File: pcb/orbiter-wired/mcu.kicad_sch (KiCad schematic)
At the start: 14 parts, among them J1 SWD, J4 AudioJack4, SW1 SW_SPDT

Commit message: Latest schematic
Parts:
- J4: LCSC Part # (none) -> C431535
- MCU1: LCSC Part # (none) -> C81720
- SW1: LCSC Part # (none) -> C221841
- USB_P1: LCSC Part # (none) -> C319148
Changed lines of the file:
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@@
+			)
+		)
+		(property "LCSC Part #" "C431535"
+			(at 128.27 35.56 0)
+			(effects
+				(font
+					(size 1.27 1.27)
+				)
+				(hide yes)
 			)
 		)
@@
 			)
 		)
+		(property "LCSC Part #" "C319148"
+			(at 110.49 76.2 0)
+			(effects
+				(font
+					(size 1.27 1.27)
+				)
+				(hide yes)
+			)
+		)
 		(pin "S1"
 		)
@@
 			)
 		)
+		(property "LCSC Part #" "C81720"
+			(at 215.9 60.96 0)
+			(effects
+				(font
+					(size 1.27 1.27)
+				)
+				(hide yes)
+			)
+		)
 		(pin "29"
 		)
@@
 			(at 217.17 146.05 0)
 			(effects
+				(font
+					(size 1.27 1.27)
+				)
+				(hide yes)
+			)
+		)
+		(property "LCSC Part #" "C221841"
+			(at 217.17 146.05 0)
+			(effects

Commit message: Orbiter wired v1.0 gerber & cleanup of old project files
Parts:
- C4: LCSC Part # C19666 -> (none)
- C5, C6, C7, C8, C9: LCSC Part # C1525 -> (none)
- J4: JLCPCB Part # C431535 -> (none); LCSC Part # C431535 -> (none)
- MCU1: JLCPCB Part # C81720 -> (none); LCSC Part # C81720 -> (none)
- R6: LCSC Part # C25744 -> (none)
- SW1: JLCPCB Part # C221841 -> (none); LCSC Part # C221841 -> (none)
- USB_P1: JLCPCB Part # C319148 -> (none); LCSC Part # C319148 -> (none)
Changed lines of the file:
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@@
-			)
-		)
-		(property "LCSC Part #" "C19666"
-			(at 195.58 125.73 0)
-			(effects
-				(font
-					(size 1.27 1.27)
-				)
-				(hide yes)
-			)
-		)
-		(property "JLCPCB Part #" ""
-			(at 195.58 125.73 0)
-			(effects
-				(font
-					(size 1.27 1.27)
-				)
-				(hide yes)
 			)
 		)
@@
 			)
 		)
-		(property "LCSC Part #" "C1525"
-			(at 242.57 125.73 0)
-			(effects
-				(font
-					(size 1.27 1.27)
-				)
-				(hide yes)
-			)
-		)
-		(property "JLCPCB Part #" ""
-			(at 242.57 125.73 0)
-			(effects
-				(font
-					(size 1.27 1.27)
-				)
-				(hide yes)
-			)
-		)
 		(pin "1"
 		)
@@
 			)
 		)
-		(property "LCSC Part #" "C1525"
-			(at 223.52 125.73 0)
-			(effects
-				(font
-					(size 1.27 1.27)
-				)
-				(hide yes)
-			)
-		)
-		(property "JLCPCB Part #" ""
-			(at 223.52 125.73 0)
-			(effects
-				(font
-					(size 1.27 1.27)
-				)
-				(hide yes)
-			)
-		)
 		(pin "1"
 		)
@@
 		)
 		(property "Description" ""
-			(at 233.045 125.73 0)
-			(effects
-				(font
-					(size 1.27 1.27)
-				)
-				(hide yes)
-			)
-		)
-		(property "LCSC Part #" "C1525"
-			(at 233.045 125.73 0)
-			(effects
-				(font
-					(size 1.27 1.27)
-				)
-				(hide yes)
-			)
-		)
-		(property "JLCPCB Part #" ""
 			(at 233.045 125.73 0)
 			(effects
@@
 			)
 		)
-		(property "JLCPCB Part #" "C431535"
-			(at 128.27 35.56 0)
-			(effects
-				(font
-					(size 1.27 1.27)
-				)
-				(hide yes)
-			)
-		)
-		(property "LCSC Part #" "C431535"
-			(at 128.27 35.56 0)
-			(effects
-				(font
-					(size 1.27 1.27)
-				)
-				(hide yes)
-			)
-		)
 		(pin "R2"
 		)
@@
 		)
 		(property "Description" ""
-			(at 85.09 34.29 0)
-			(effects
-				(font
-					(size 1.27 1.27)
-				)
-				(hide yes)
-			)
-		)
-		(property "JLCPCB Part #" ""
 			(at 85.09 34.29 0)
 			(effects
@@
 			)
 		)
-		(property "JLCPCB Part #" ""
-			(at 153.67 34.29 0)
-			(effects
-				(font
-					(size 1.27 1.27)
-				)
-				(hide yes)
-			)
-		)
 		(pin "2"
 		)
@@
 		)
 		(property "Description" ""
-			(at 204.47 125.73 0)
-			(effects
-				(font
-					(size 1.27 1.27)
-				)
-				(hide yes)
-			)
-		)
-		(property "LCSC Part #" "C1525"
-			(at 204.47 125.73 0)
-			(effects
-				(font
-					(size 1.27 1.27)
-				)
-				(hide yes)
-			)
-		)
-		(property "JLCPCB Part #" ""
 			(at 204.47 125.73 0)
 			(effects
@@
 			)
 		)
-		(property "JLCPCB Part #" "C319148"
-			(at 110.49 76.2 0)
-			(effects
-				(font
-					(size 1.27 1.27)
-				)
-				(hide yes)
-			)
-		)
-		(property "LCSC Part #" "C319148"
-			(at 110.49 76.2 0)
-			(effects
-				(font
-					(size 1.27 1.27)
-				)
-				(hide yes)
-			)
-		)
 		(pin "S1"
 		)
@@
 			)
 		)
-		(property "JLCPCB Part #" "C81720"
-			(at 215.9 60.96 0)
-			(effects
-				(font
-					(size 1.27 1.27)
-				)
-				(hide yes)
-			)
-		)
-		(property "LCSC Part #" "C81720"
-			(at 215.9 60.96 0)
-			(effects
-				(font
-					(size 1.27 1.27)
-				)
-				(hide yes)
-			)
-		)
 		(pin "29"
 		)
@@
 			)
 		)
-		(property "LCSC Part #" "C1525"
-			(at 213.995 125.73 0)
-			(effects
-				(font
-					(size 1.27 1.27)
-				)
-				(hide yes)
-			)
-		)
-		(property "JLCPCB Part #" ""
-			(at 213.995 125.73 0)
-			(effects
-				(font
-					(size 1.27 1.27)
-				)
-				(hide yes)
-			)
-		)
 		(pin "2"
 		)
@@
 		)
 		(property "Description" ""
-			(at 209.55 146.05 0)
-			(effects
-				(font
-					(size 1.27 1.27)
-				)
-				(hide yes)
-			)
-		)
-		(property "LCSC Part #" "C25744"
-			(at 209.55 146.05 0)
-			(effects
-				(font
-					(size 1.27 1.27)
-				)
-				(hide yes)
-			)
-		)
-		(property "JLCPCB Part #" ""
 			(at 209.55 146.05 0)
 			(effects
@@
 			)
 		)
-		(property "JLCPCB Part #" ""
-			(at 128.27 66.04 0)
-			(effects
-				(font
-					(size 1.27 1.27)
-				)
-				(hide yes)
-			)
-		)
 		(pin "2"
 		)
@@
 			(at 217.17 146.05 0)
 			(effects
-				(font
-					(size 1.27 1.27)
-				)
-				(hide yes)
-			)
-		)
-		(property "JLCPCB Part #" "C221841"
-			(at 217.17 146.05 0)
-			(effects
-				(font
-					(size 1.27 1.27)
-				)
-				(hide yes)
-			)
-		)
-		(property "LCSC Part #" "C221841"
-			(at 217.17 146.05 0)
-			(effects

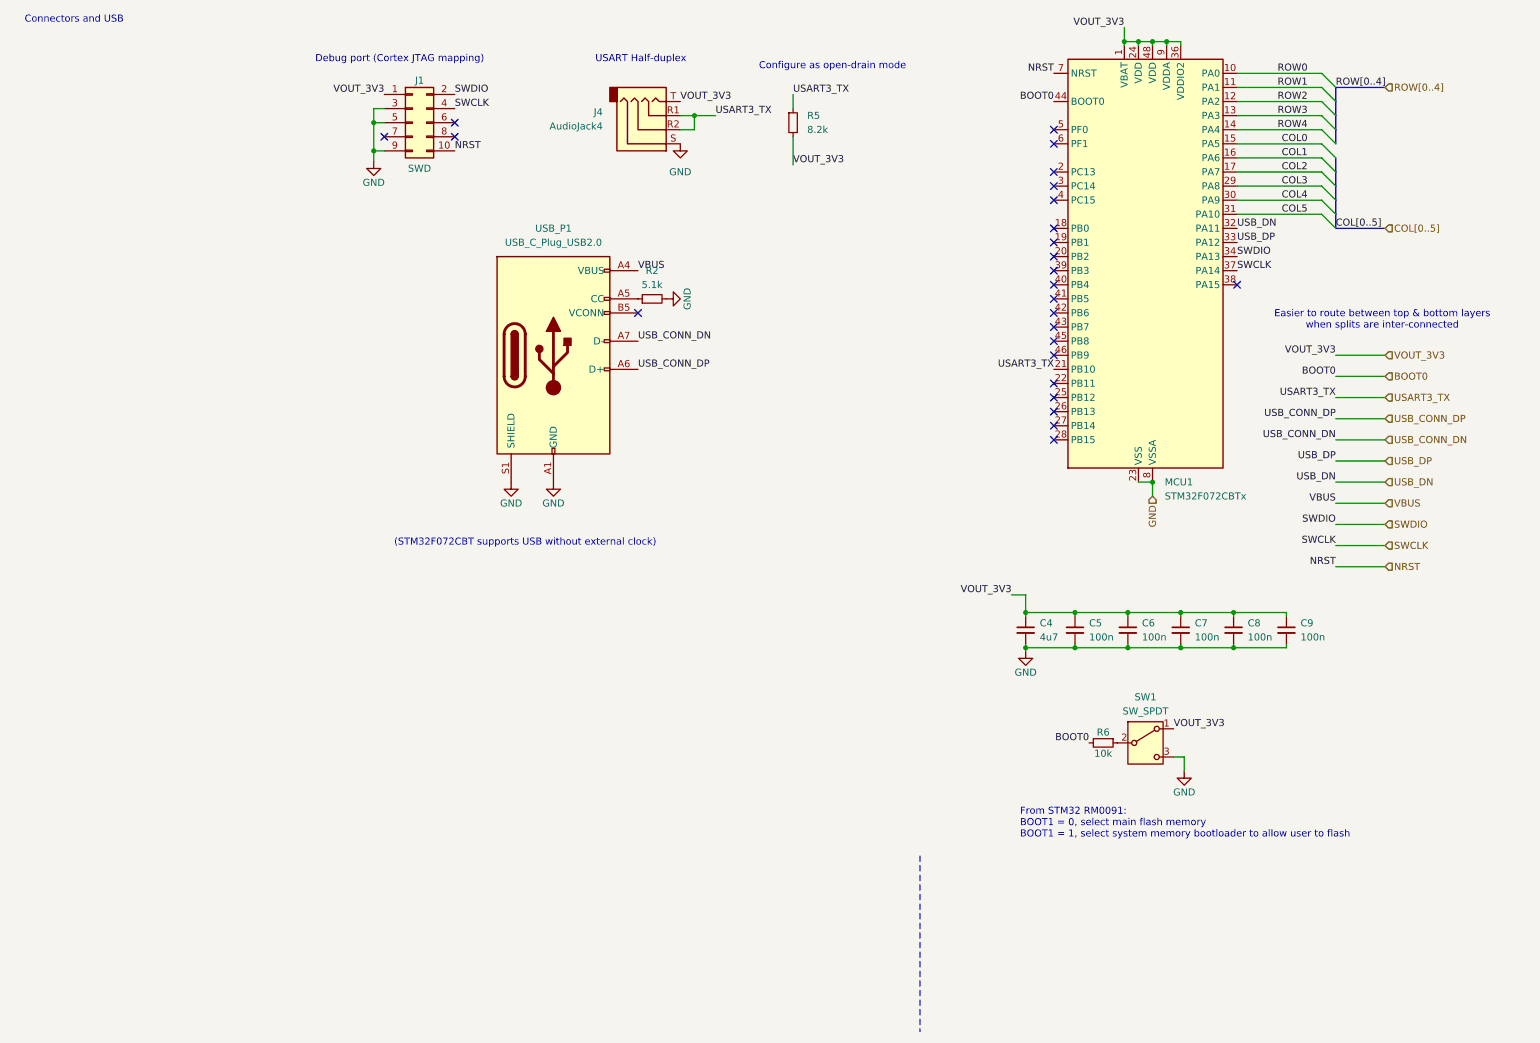
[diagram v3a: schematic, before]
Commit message: WIP prepare component placement for standalone dev pcb
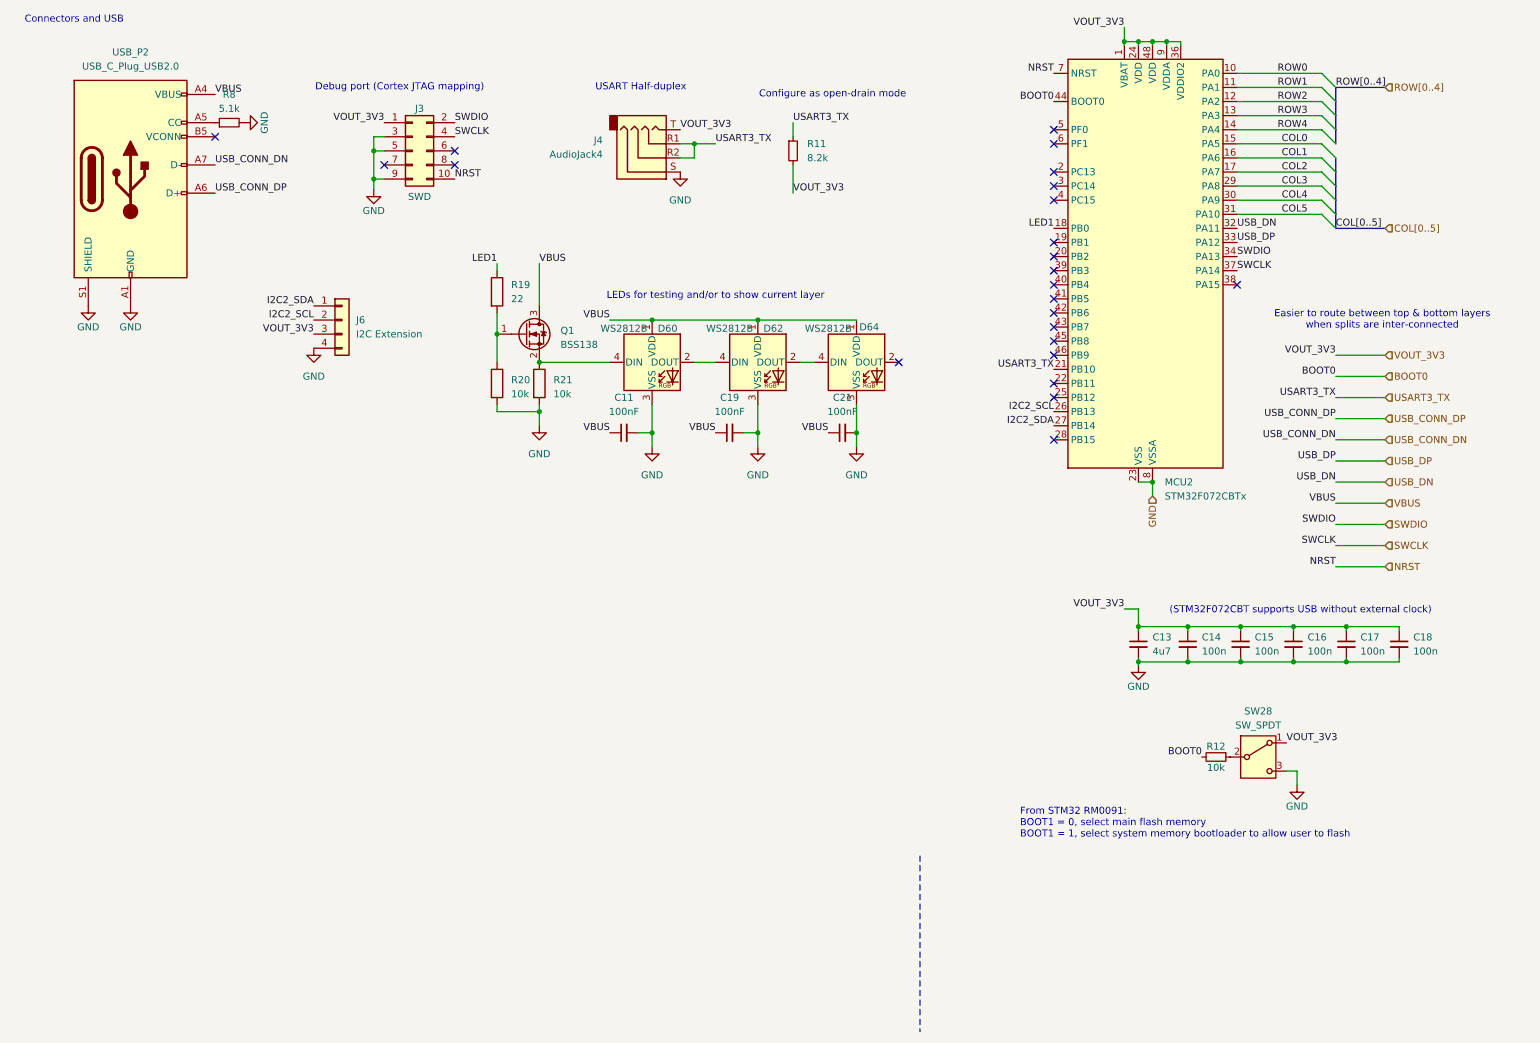
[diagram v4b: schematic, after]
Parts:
- added C11, C19, C21: 100nF, Capacitor_SMD:C_0603_1608Metric_Pad1.08x0.95mm_HandSolder, symbol Device:C_Small
- added D60, D62, D64: WS2812B, LED_SMD:LED_WS2812B-2020_PLCC4_2.0x2.0mm, symbol LED:WS2812B
- added J6: I2C Extension, Connector_PinSocket_1.00mm:PinSocket_1x04_P1.00mm_Vertical_SMD_Pin1Left, symbol Connector_Generic:Conn_01x04
- added Q1: BSS138, Package_TO_SOT_SMD:SOT-23, symbol Transistor_FET:BSS138
- added R19: 22, Resistor_SMD:R_0603_1608Metric, symbol Device:R
- added R20, R21: 10k, Resistor_SMD:R_0603_1608Metric, symbol Device:R
- renumbered C4 to C13, C5 to C14, C6 to C15, C7 to C16, C8 to C17, C9 to C18, J1 to J3, MCU1 to MCU2, R5 to R11, R6 to R12, R2 to R8, SW1 to SW28, USB_P1 to USB_P2
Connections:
- net GND: now also C11.2, C19.2, C21.2, D60.3 (VSS), D62.3 (VSS), D64.3 (VSS), J6.4 (Pin_4), R20.2, R21.2
- net VBUS: now also C11.1, C19.1, C21.1, D60.1 (VDD), D62.1 (VDD), D64.1 (VDD), Q1.3 (D)
- net VOUT_3V3: now also J6.3 (Pin_3)
- net LED1: now reaches MCU2.18 (PB0)
- net LED1: now also R19.1
- net I2C2_SCL: now reaches MCU2.26 (PB13)
- net I2C2_SCL: now also J6.2 (Pin_2)
- net I2C2_SDA: now reaches MCU2.27 (PB14)
- net I2C2_SDA: now also J6.1 (Pin_1)
- new net: Q1.1 (G), R19.2, R20.1
- new net: D60.4 (DIN), Q1.2 (S), R21.1
- new net: D62.2 (DOUT), D64.4 (DIN)
- new net: D60.2 (DOUT), D62.4 (DIN)
- no-connect marks 25 -> 23
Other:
- note added: "LEDs for testing and/or to show current layer"
- moved on the sheet: C13, C14, C15, C16, C17, C18, J3, J4, R11, R12, R8, SW28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

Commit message: Latest WIP
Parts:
- removed J3: SWD, Connector_PinSocket_1.27mm:PinSocket_2x05_P1.27mm_Vertical_SMD, symbol Connector_Generic:Conn_02x05_Odd_Even
- removed J6: I2C Extension, Connector_PinSocket_1.00mm:PinSocket_1x04_P1.00mm_Vertical_SMD_Pin1Left, symbol Connector_Generic:Conn_01x04
- removed R12: 10k, Resistor_SMD:R_0603_1608Metric, symbol Device:R_Small
- removed SW28: SW_SPDT, Button_Switch_SMD:SW_SPDT_PCM12, symbol Switch:SW_SPDT
- added R6: 10k, Resistor_SMD:R_0603_1608Metric, symbol Device:R_Small
- added SW1: SW_SPDT, Button_Switch_SMD:SW_SPDT_PCM12, symbol Switch:SW_SPDT
- renumbered Q1 to Q2
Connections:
- net BOOT0: now also R6.2
- net GND: now also SW1.3 (C)
- net USART3_TX: no longer J4.R2
- net VOUT_3V3: now also SW1.1 (A)
- net USART3_RX: now reaches MCU2.22 (PB11)
- net USART3_RX: now also J4.R2
- new net: R6.1, SW1.2 (B)
- no-connect marks 23 -> 19
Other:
- note removed: "Debug port (Cortex JTAG mapping)"
- moved on the sheet: C13, C14, C15, C16, C17, C18, R8, USB_P2

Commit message: No DRC errors with new clean layout
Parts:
- SW28: renamed from SW1; footprint Button_Switch_SMD:SW_SPDT_PCM12 -> Button_Switch_SMD:SW_SPST_PTS647_Sx38
- renumbered R6 to R7
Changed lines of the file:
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@@
 		(on_board yes)
 		(dnp no)
-		(property "Reference" "#PWR012"
+		(property "Reference" "#PWR018"
 			(at 79.375 134.62 0)
 			(effects
@@
 		(on_board yes)
 		(dnp no)
-		(property "Reference" "R6"
+		(property "Reference" "R7"
 			(at 64.77 121.285 90)
 			(effects
@@
 		(on_board yes)
 		(dnp no)
-		(property "Reference" "SW1"
+		(property "Reference" "SW28"
 			(at 72.39 114.935 0)
 			(effects
@@
 			)
 		)
-		(property "Footprint" "Button_Switch_SMD:SW_SPDT_PCM12"
+		(property "Footprint" "Button_Switch_SMD:SW_SPST_PTS647_Sx38"
 			(at 72.39 123.19 0)
 			(effects

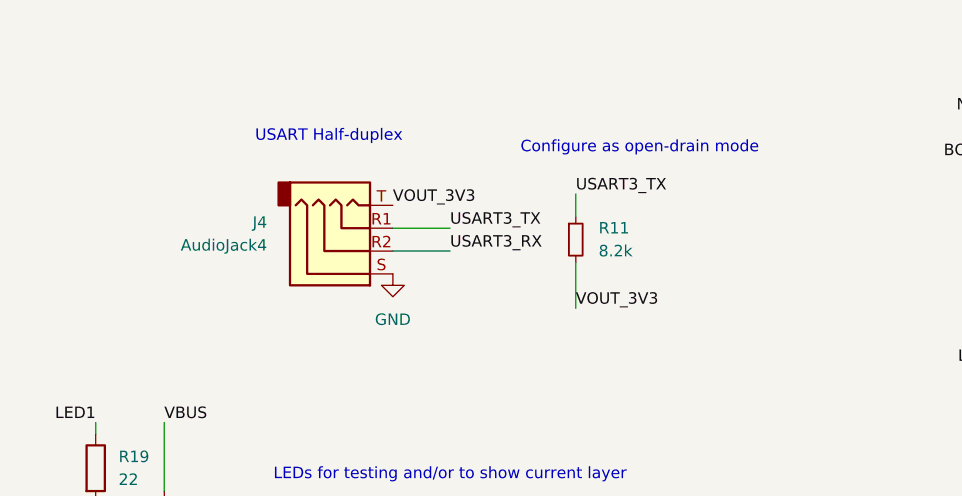
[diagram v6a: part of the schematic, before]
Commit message: Add pull-up for UART RX as well
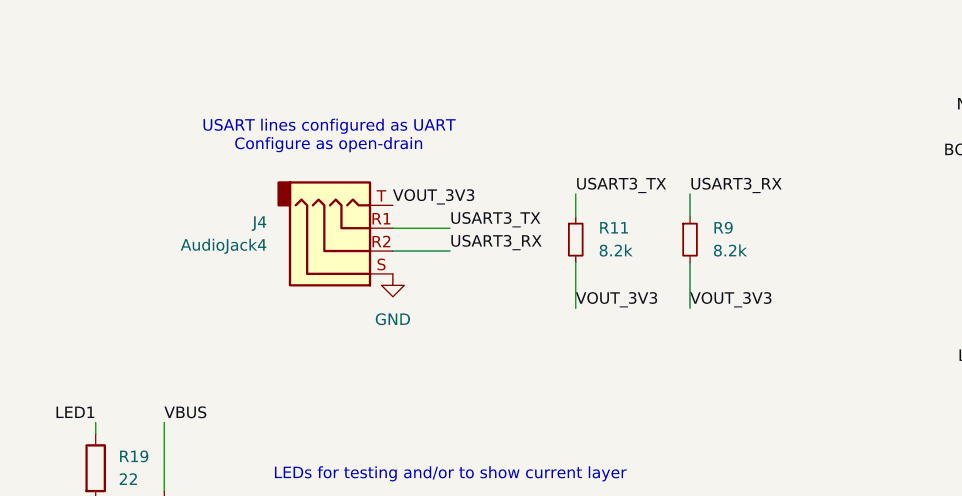
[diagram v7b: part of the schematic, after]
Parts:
- added R9: 8.2k, Resistor_SMD:R_0603_1608Metric, symbol Device:R_Small
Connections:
- net USART3_RX: now also R9.1
- net VOUT_3V3: now also R9.2
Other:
- note added: "USART lines configured as UART Configure as open-drain"
- note removed: "Configure as open-drain mode"
- note removed: "USART Half-duplex"
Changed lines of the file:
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@@
 	(wire
 		(pts
+			(xy 166.37 34.29) (xy 166.37 36.83)
+		)
+		(stroke
+			(width 0)
+			(type default)
+		)
+	)
+	(wire
+		(pts
 			(xy 114.3 121.285) (xy 114.3 121.92)
 		)
@@
 	(wire
 		(pts
+			(xy 166.37 41.91) (xy 166.37 46.99)
+		)
+		(stroke
+			(width 0)
+			(type default)
+		)
+	)
+	(wire
+		(pts
 			(xy 248.92 45.72) (xy 233.68 45.72)
 		)
@@
 		)
 	)
-	(text "Configure as open-drain mode"
-		(exclude_from_sim no)
-		(at 160.782 29.21 0)
-		(effects
-			(font
-				(size 1.27 1.27)
-			)
-		)
-	)
-	(text "USART Half-duplex "
+	(text "USART lines configured as UART\nConfigure as open-drain"
 		(exclude_from_sim no)
 		(at 126.238 27.94 0)
@@
 		)
 	)
+	(label "USART3_RX"
+		(at 166.37 34.29 0)
+		(fields_autoplaced yes)
+		(effects
+			(font
+				(size 1.27 1.27)
+			)
+			(justify left bottom)
+		)
+	)
 	(label "USB_CONN_DN"
 		(at 251.46 95.25 180)
@@
 		)
 	)
+	(label "VOUT_3V3"
+		(at 166.37 46.99 0)
+		(fields_autoplaced yes)
+		(effects
+			(font
+				(size 1.27 1.27)
+			)
+			(justify left bottom)
+		)
+	)
 	(label "COL[0..5]"
 		(at 251.46 53.34 0)
@@
 					(unit 1)
 				)
+			)
+		)
+	)
+	(symbol
+		(lib_id "Device:R_Small")
+		(at 166.37 39.37 0)
+		(unit 1)
+		(exclude_from_sim no)
+		(in_bom yes)
+		(on_board yes)
+		(dnp no)
+		(fields_autoplaced yes)
+		(property "Reference" "R9"
+			(at 168.91 38.0999 0)
+			(effects
+				(font
+					(size 1.27 1.27)
+				)
+				(justify left)
+			)
+		)
+		(property "Value" "8.2k"
+			(at 168.91 40.6399 0)
+			(effects
+				(font
+					(size 1.27 1.27)
+				)
+				(justify left)
+			)
+		)
+		(property "Footprint" "Resistor_SMD:R_0603_1608Metric"
+			(at 166.37 39.37 0)
+			(effects
+				(font
+					(size 1.27 1.27)
+				)
+				(hide yes)
+			)
+		)
+		(property "Datasheet" "~"
+			(at 166.37 39.37 0)
+			(effects
+				(font
+					(size 1.27 1.27)
+				)
+				(hide yes)
+			)
+		)
+		(property "Description" "Resistor, small symbol"
+			(at 166.37 39.37 0)
+			(effects
+				(font
+					(size 1.27 1.27)
+				)
+				(hide yes)
+			)
+		)
+		(pin "2"
+		)
+		(pin "1"
+		)
+		(instances
+			(project "orbiter"
+				(path "/623f70b3-6381-43ff-98c1-e36c34bee313/c14a50ad-c630-40dd-ac14-b3b40c9c245d"
+					(reference "R10")
+					(unit 1)
+				)
+				(path "/623f70b3-6381-43ff-98c1-e36c34bee313/e058b5b4-db4d-4bc7-8f42-8e3bd37c89bf"
+					(reference "R9")
+					(unit 1)
+				)
